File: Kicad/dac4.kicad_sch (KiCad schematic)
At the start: 10 parts

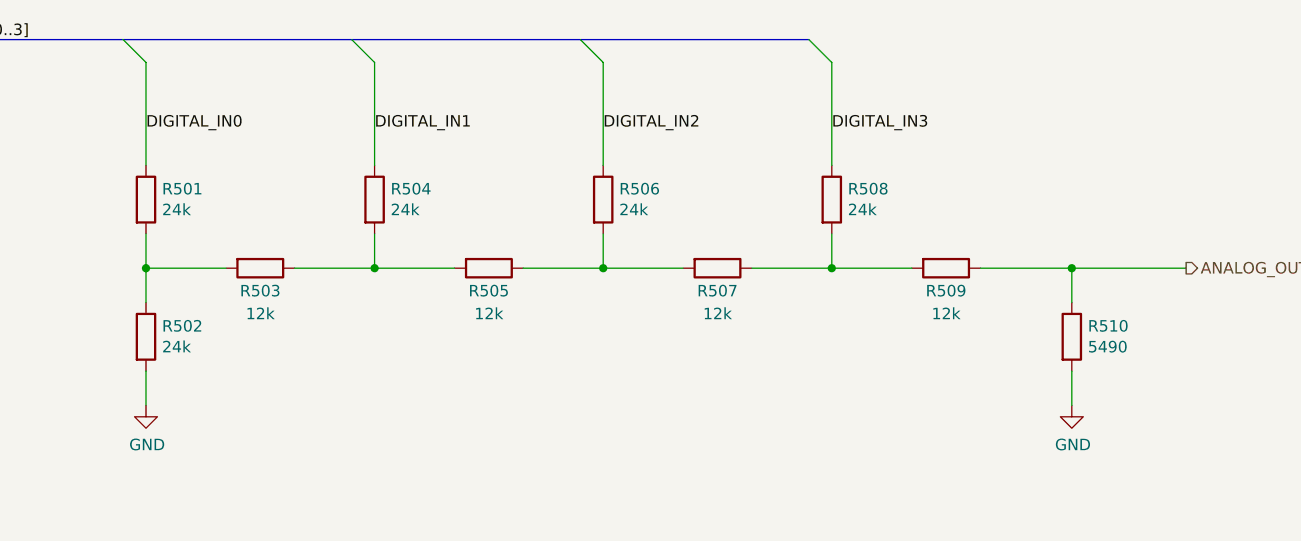
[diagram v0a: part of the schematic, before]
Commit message: Retitle sheets and renumber parts.
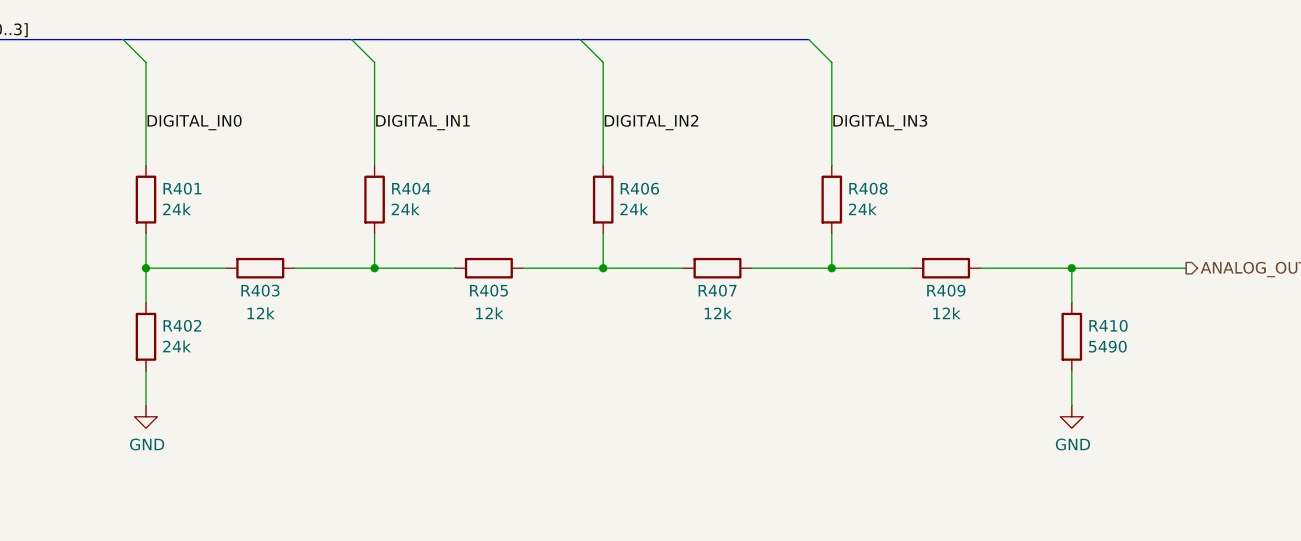
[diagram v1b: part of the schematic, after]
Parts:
- renumbered R501 to R401, R502 to R402, R503 to R403, R504 to R404, R505 to R405, R506 to R406, R507 to R407, R508 to R408, R509 to R409, R510 to R410
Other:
- company: https://neotron-compute.github.io/ -> https://neotron-compute.github.io
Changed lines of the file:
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@@
     (date "${date}")
     (rev "${version}")
-    (company "https://neotron-compute.github.io/")
-    (comment 1 "Licenced as CC BY-SA")
+    (company "https://neotron-compute.github.io")
+    (comment 1 "Licensed as CC-BY-SA")
     (comment 2 "Copyright (c) The Neotron Developers, 2022")
   )
@@
   (symbol (lib_id "Device:R") (at 88.9 68.58 0) (unit 1)
     (in_bom yes) (on_board yes)
-    (property "Reference" "R501" (id 0) (at 90.678 67.4116 0)
+    (property "Reference" "R401" (id 0) (at 90.678 67.4116 0)
       (effects (font (size 1.27 1.27)) (justify left))
     )
@@
   (symbol (lib_id "Device:R") (at 165.1 68.58 0) (unit 1)
     (in_bom yes) (on_board yes)
-    (property "Reference" "R508" (id 0) (at 166.878 67.4116 0)
+    (property "Reference" "R408" (id 0) (at 166.878 67.4116 0)
       (effects (font (size 1.27 1.27)) (justify left))
     )
@@
   (symbol (lib_id "Device:R") (at 101.6 76.2 270) (unit 1)
     (in_bom yes) (on_board yes)
-    (property "Reference" "R503" (id 0) (at 101.6 78.74 90))
+    (property "Reference" "R403" (id 0) (at 101.6 78.74 90))
     (property "Value" "12k" (id 1) (at 101.6 81.28 90))
     (property "Footprint" "Resistor_SMD:R_0805_2012Metric_Pad1.20x1.40mm_HandSolder" (id 2) (at 101.6 74.422 90)
@@
   (symbol (lib_id "Device:R") (at 114.3 68.58 0) (unit 1)
     (in_bom yes) (on_board yes)
-    (property "Reference" "R504" (id 0) (at 116.078 67.4116 0)
+    (property "Reference" "R404" (id 0) (at 116.078 67.4116 0)
       (effects (font (size 1.27 1.27)) (justify left))
     )
@@
   (symbol (lib_id "Device:R") (at 127 76.2 270) (unit 1)
     (in_bom yes) (on_board yes)
-    (property "Reference" "R505" (id 0) (at 127 78.74 90))
+    (property "Reference" "R405" (id 0) (at 127 78.74 90))
     (property "Value" "12k" (id 1) (at 127 81.28 90))
     (property "Footprint" "Resistor_SMD:R_0805_2012Metric_Pad1.20x1.40mm_HandSolder" (id 2) (at 127 74.422 90)
@@
   (symbol (lib_id "Device:R") (at 152.4 76.2 270) (unit 1)
     (in_bom yes) (on_board yes)
-    (property "Reference" "R507" (id 0) (at 152.4 78.74 90))
+    (property "Reference" "R407" (id 0) (at 152.4 78.74 90))
     (property "Value" "12k" (id 1) (at 152.4 81.28 90))
     (property "Footprint" "Resistor_SMD:R_0805_2012Metric_Pad1.20x1.40mm_HandSolder" (id 2) (at 152.4 74.422 90)
@@
   (symbol (lib_id "Device:R") (at 177.8 76.2 270) (unit 1)
     (in_bom yes) (on_board yes)
-    (property "Reference" "R509" (id 0) (at 177.8 78.74 90))
+    (property "Reference" "R409" (id 0) (at 177.8 78.74 90))
     (property "Value" "12k" (id 1) (at 177.8 81.28 90))
     (property "Footprint" "Resistor_SMD:R_0805_2012Metric_Pad1.20x1.40mm_HandSolder" (id 2) (at 177.8 74.422 90)
@@
   (symbol (lib_id "Device:R") (at 191.77 83.82 0) (unit 1)
     (in_bom yes) (on_board yes)
-    (property "Reference" "R510" (id 0) (at 193.548 82.6516 0)
+    (property "Reference" "R410" (id 0) (at 193.548 82.6516 0)
       (effects (font (size 1.27 1.27)) (justify left))
     )
@@
   (symbol (lib_id "power:GND") (at 88.9 91.44 0) (unit 1)
     (in_bom yes) (on_board yes)
-    (property "Reference" "#PWR0501" (id 0) (at 88.9 97.79 0)
+    (property "Reference" "#PWR0401" (id 0) (at 88.9 97.79 0)
       (effects (font (size 1.27 1.27)) hide)
     )
@@
   (symbol (lib_id "power:GND") (at 191.77 91.44 0) (unit 1)
     (in_bom yes) (on_board yes)
-    (property "Reference" "#PWR0502" (id 0) (at 191.77 97.79 0)
+    (property "Reference" "#PWR0402" (id 0) (at 191.77 97.79 0)
       (effects (font (size 1.27 1.27)) hide)
     )
@@
   (symbol (lib_id "Device:R") (at 88.9 83.82 0) (unit 1)
     (in_bom yes) (on_board yes)
-    (property "Reference" "R502" (id 0) (at 90.678 82.6516 0)
+    (property "Reference" "R402" (id 0) (at 90.678 82.6516 0)
       (effects (font (size 1.27 1.27)) (justify left))
     )
@@
   (symbol (lib_id "Device:R") (at 139.7 68.58 0) (unit 1)
     (in_bom yes) (on_board yes)
-    (property "Reference" "R506" (id 0) (at 141.478 67.4116 0)
-      (effects (font (size 1.27 1.27)) (justify left))
-    )
+    (property "Reference" "R406" (id 0) (at 141.478 67.4116 0)
+      (effects (font (size 1.27 1.27)) (justify left))
+    )

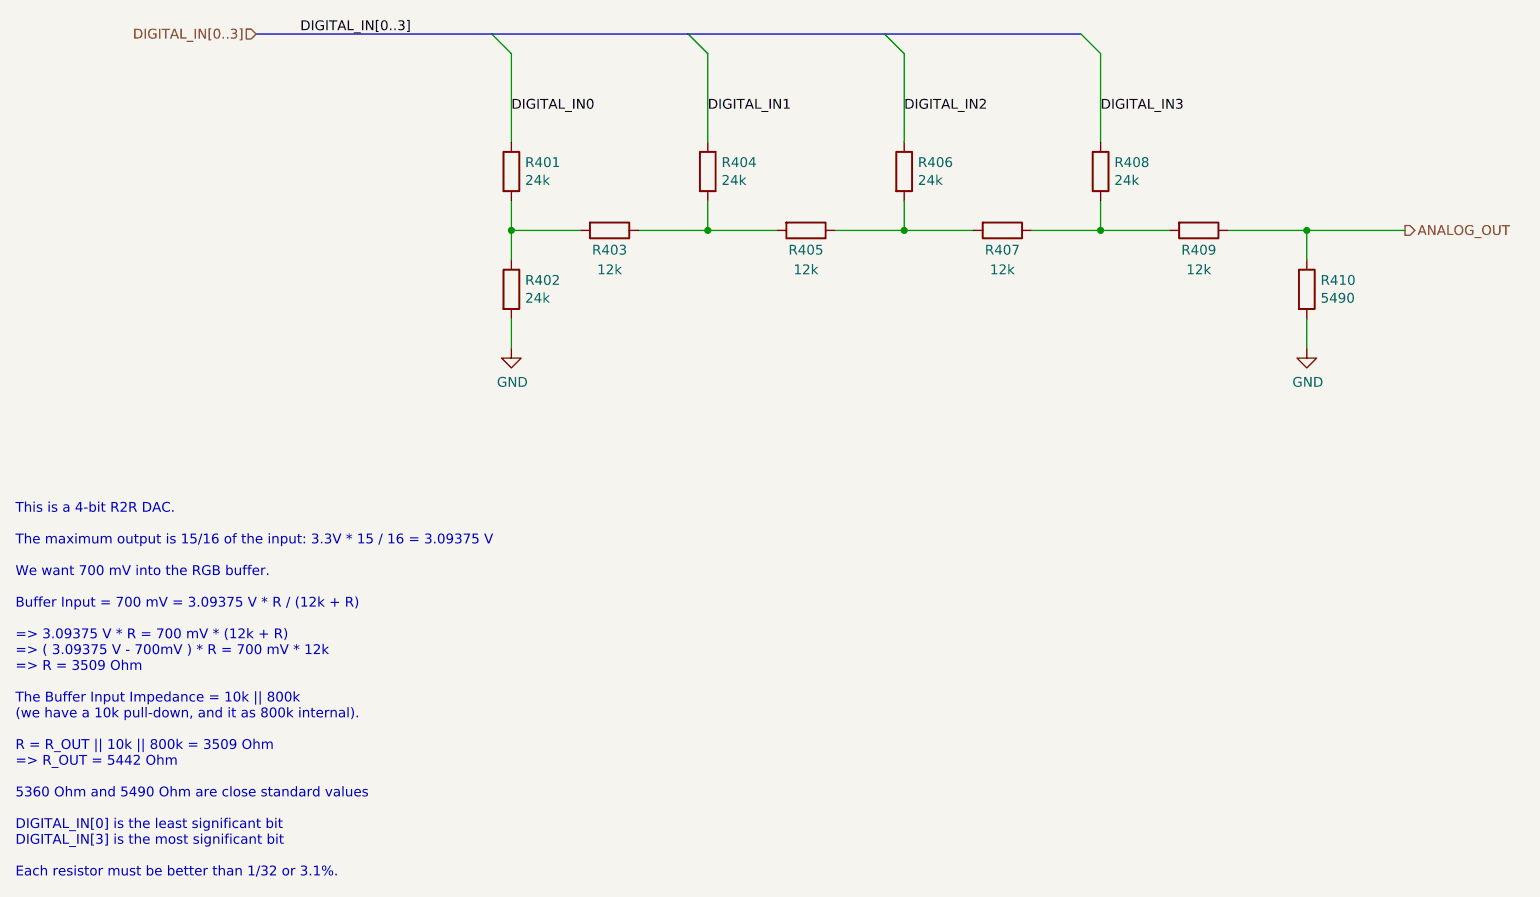
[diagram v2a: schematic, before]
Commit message: Set DAC to 1k/2k. Closes #77 Replaced some CPL resistors. Partial fix for #83 Added bridges for VGA I2C if ESD chip not fitted. Closes #51
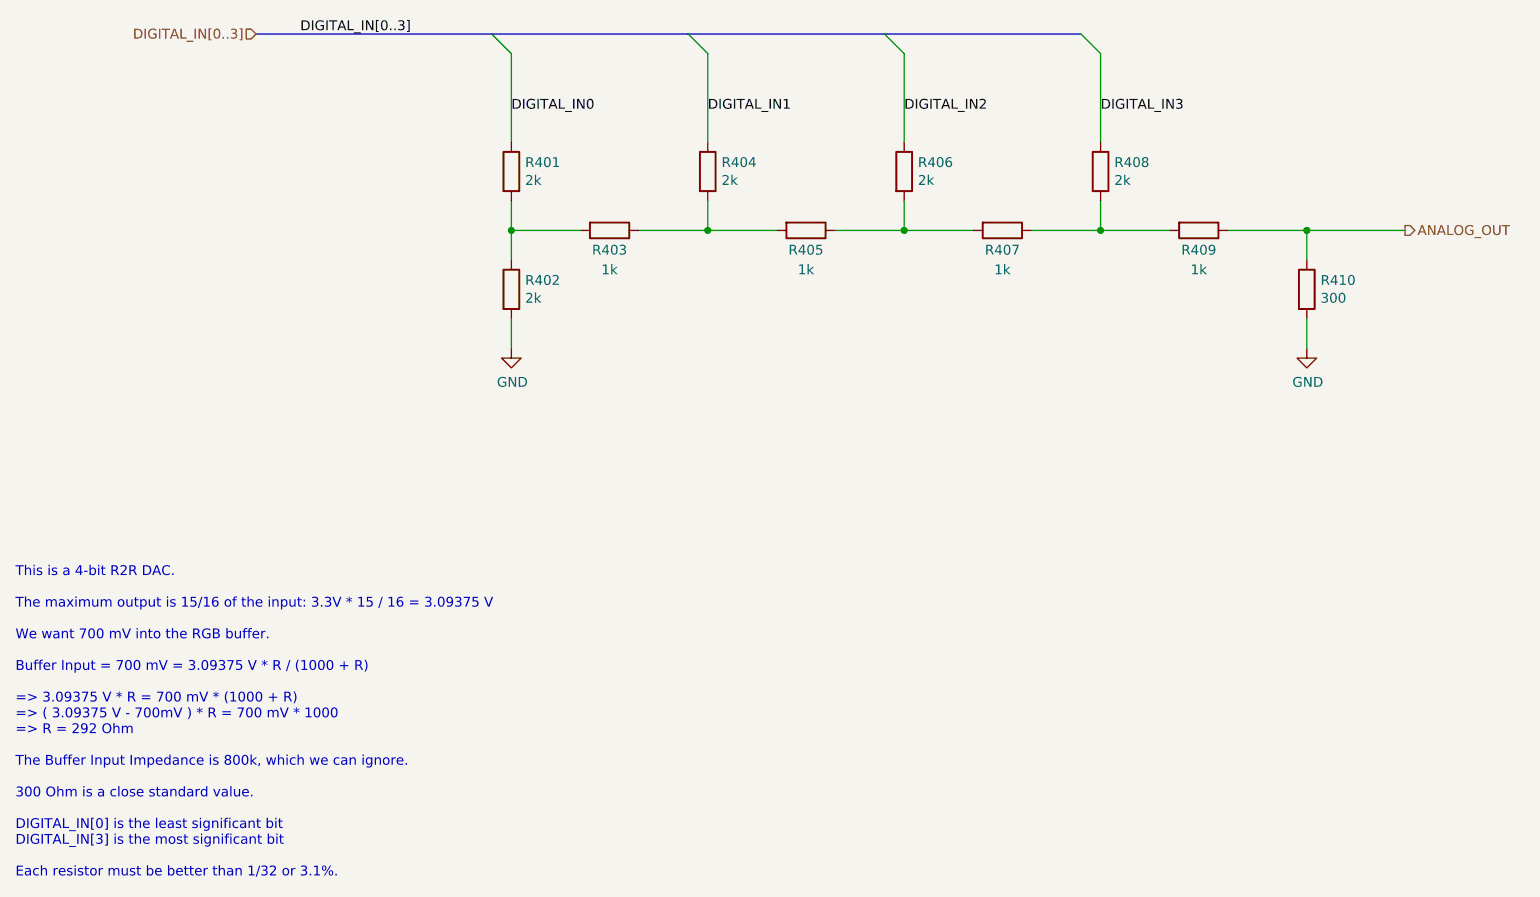
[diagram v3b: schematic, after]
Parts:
- R401, R402, R404, R406, R408: value 24k -> 2k; Digikey RNCF0805DTE24K0CT-ND -> RMCF0805FT2K00CT-ND; LCSC Part# C17575 -> C17604; MPN RMCF0805FT24K0 -> RMCF0805FT2K00
- R403, R405, R407, R409: value 12k -> 1k; Digikey RNCF0805DTE12K0CT-ND -> RMCF0805FT1K00CT-ND; LCSC Part# C97163 -> C17513; MPN RMCF0805FT12K0 -> RMCF0805FT1K00
- R410: value 5490 -> 300; Digikey RNCF0805DTE5K49CT-ND -> RMCF0805FT300RCT-ND; LCSC Part# C17726 -> C17617; MPN RMCF0805FT5K49 -> RMCF0805FT300R
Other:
- note added: "This is a 4-bit R2R DAC. The maximum output is 15/16 of the input: 3.3V * 15 / 16 = 3.09375 V We want 700 mV into the RGB buffer. Buffer Input = 700 mV = 3.09375 V * R / (1000 + R) => 3.09375 V * R = 700 mV * (1000 + R) => ( 3.09375 V - 700mV ) * R = 700 mV * 1000 => R = 292 Ohm The Buffer Input Impedance is 800k, which we can ignore. 300 Ohm is a close standard value. DIGITAL_IN[0] is the least 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"
- note removed: "This is a 4-bit R2R DAC. The maximum output is 15/16 of the input: 3.3V * 15 / 16 = 3.09375 V We want 700 mV into the RGB buffer. Buffer Input = 700 mV = 3.09375 V * R / (12k + R) => 3.09375 V * R = 700 mV * (12k + R) => ( 3.09375 V - 700mV ) * R = 700 mV * 12k => R = 3509 Ohm The Buffer Input Impedance = 10k || 800k (we have a 10k pull-down, and it as 800k internal). R = R_OUT || 10k || 800k = 3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"
